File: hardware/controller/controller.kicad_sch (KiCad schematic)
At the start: 29 parts, among them J1 DC_12V_IN, J2 HDD_POWER_OUT, J3 470531000, J4 470531000, J5 Conn_01x07, Q1 2N3904, Q2 2N3904, U1 TSR0.5-2450, U2 XIAO-RP2350-SMD, U3 INA228, U4 74HC4051

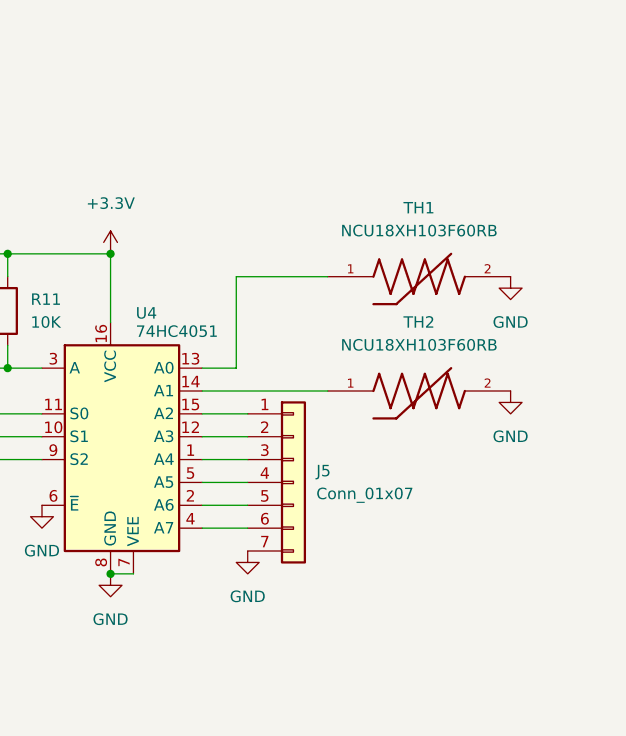
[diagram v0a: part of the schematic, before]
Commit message: swap out thermistor connector
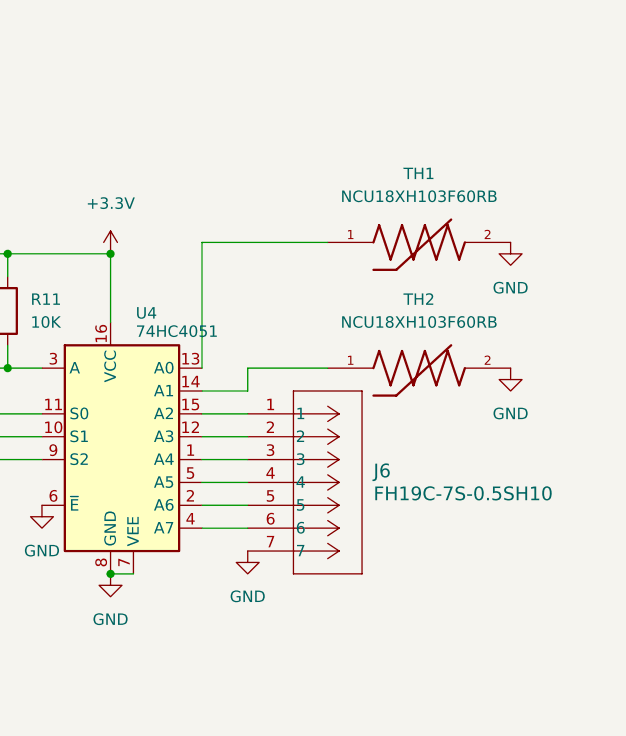
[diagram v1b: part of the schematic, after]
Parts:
- removed J5: Conn_01x07, Connector_JST:JST_XH_B7B-XH-A_1x07_P2.50mm_Vertical, symbol Connector_Generic:Conn_01x07
- added J6: FH19C-7S-0.5SH10, CONN7_FH19C_7S_HIR, symbol Hirose_2026-10-24_22-08-50:FH19C-7S-0.5SH10
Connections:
- net GND: now also J6.7
- net at U4.1 (A4): now also J6.3
- net at U4.12 (A3): now also J6.2
- net at U4.15 (A2): now also J6.1
- net at U4.2 (A6): now also J6.5
- net at U4.4 (A7): now also J6.6
- net at U4.5 (A5): now also J6.4
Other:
- moved on the sheet: TH1, TH2

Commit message: update symbol and footprint libraries for thermistor strip
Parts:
- J6: footprint CONN7_FH19C_7S_HIR -> Hirose_FH19C_7S_0_5SH:CONN7_FH19C_7S_HIR
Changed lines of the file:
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@@
 			)
 		)
-		(property "Footprint" "CONN7_FH19C_7S_HIR"
+		(property "Footprint" "Hirose_FH19C_7S_0_5SH:CONN7_FH19C_7S_HIR"
 			(at 213.36 124.46 0)
 			(hide yes)

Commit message: fix shunt footprint
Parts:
- removed RSH1: 0.2m, CSS2H_3920R_L200F:RES_3920R_L200x_BRN, symbol CSS2H_3920R_L200F:CSS2H-3920R-L200F
- added RSH1: CRF2512-FZ-R001ELF, CRF2512-FZ-R001ELF:RESC6432X80N, symbol CRF2512-FZ-R001ELF:CRF2512-FZ-R001ELF
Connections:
- net 12V_HDD: now also RSH1.2
- net 12V_IN: now also RSH1.1
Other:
- moved on the sheet: R3

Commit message: first pass at placing components for fan controller on front face
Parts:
- RSH1: footprint CRF2512-FZ-R001ELF:RESC6432X80N -> CRF2512_FZ_R001ELF:RESC6432X80N
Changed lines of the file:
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@@
 			)
 		)
-		(property "Footprint" "CRF2512-FZ-R001ELF:RESC6432X80N"
+		(property "Footprint" "CRF2512_FZ_R001ELF:RESC6432X80N"
 			(at 152.4 59.69 0)
 			(hide yes)

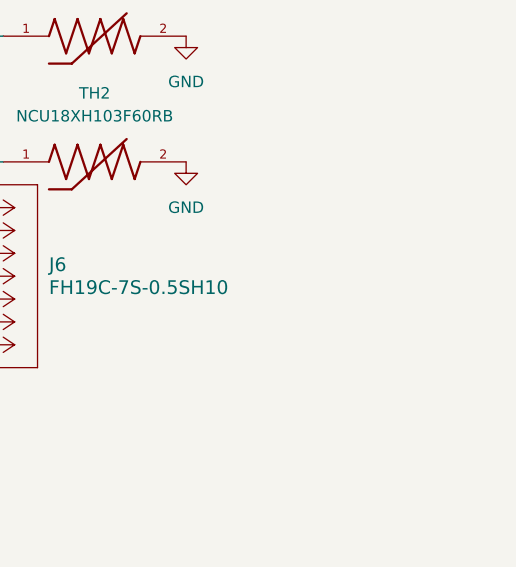
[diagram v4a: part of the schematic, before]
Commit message: initial attempt at tracing for controller, still need vias
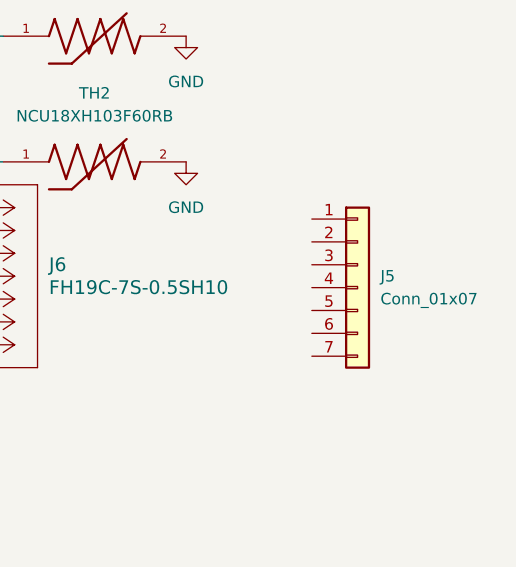
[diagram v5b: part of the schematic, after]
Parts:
- added J5: Conn_01x07, symbol Connector_Generic:Conn_01x07
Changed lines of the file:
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@@
+	)
+	(symbol
+		(lib_id "Connector_Generic:Conn_01x07")
+		(at 261.62 133.35 0)
+		(unit 1)
+		(body_style 1)
+		(exclude_from_sim no)
+		(in_bom yes)
+		(on_board yes)
+		(in_pos_files yes)
+		(dnp no)
+		(fields_autoplaced yes)
+		(property "Reference" "J5"
+			(at 264.16 132.0799 0)
+			(show_name no)
+			(do_not_autoplace no)
+			(effects
+				(font
+					(size 1.27 1.27)
+				)
+				(justify left)
+			)
+		)
+		(property "Value" "Conn_01x07"
+			(at 264.16 134.6199 0)
+			(show_name no)
+			(do_not_autoplace no)
+			(effects
+				(font
+					(size 1.27 1.27)
+				)
+				(justify left)
+			)
+		)
+		(property "Footprint" ""
+			(at 261.62 133.35 0)
+			(hide yes)
+			(show_name no)
+			(do_not_autoplace no)
+			(effects
+				(font
+					(size 1.27 1.27)
+				)
+			)
+		)
+		(property "Datasheet" ""
+			(at 261.62 133.35 0)
+			(hide yes)
+			(show_name no)
+			(do_not_autoplace no)
+			(effects
+				(font
+					(size 1.27 1.27)
+				)
+			)
+		)
+		(property "Description" "Generic connector, single row, 01x07, script generated (kicad-library-utils/schlib/autogen/connector/)"
+			(at 261.62 133.35 0)
+			(hide yes)
+			(show_name no)
+			(do_not_autoplace no)
+			(effects
+				(font
+					(size 1.27 1.27)
+				)
+			)
+		)
+		(pin "2"
+		)
+		(pin "1"
+		)
+		(pin "3"
+		)
+		(pin "4"
+		)
+		(pin "7"
+		)
+		(pin "6"
+		)
+		(pin "5"
+		)
+		(instances
+			(project "controller"
+				(path "/2efa048c-d6c1-446c-ae8e-880d974401eb"
+					(reference "J5")
+					(unit 1)
+				)
+			)
+		)
 	)
 	(symbol

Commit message: finish routes for INA228
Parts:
- added NT1, NT2: NetTie_2, NetTie:NetTie-2_SMD_Pad0.5mm, symbol Device:NetTie_2
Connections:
- net 12V_HDD: now also RSH1.1, NT2.1; no longer R4.1, RSH1.2, U3.8 (Vbus)
- net 12V_IN: now also RSH1.2, NT1.1; no longer R3.1, RSH1.1
- net FAN1_PWM: now also U2.9 (D8); no longer U2.8 (D7)
- net FAN1_TACH: now also U2.8 (D7); no longer U2.9 (D8)
- net FAN2_PWM: now also U2.11 (D10); no longer U2.10 (D9)
- net FAN2_TACH: now also U2.10 (D9); no longer U2.11 (D10)
- net NTC_SEL0: now also U2.7 (D6); no longer U2.3 (D2)
- net NTC_SEL2: now also U2.3 (D2); no longer U2.7 (D6)
- new net 12V_HDD_SENSE: NT2.2, R4.1, U3.8 (Vbus)
- new net 12V_IN_SENSE: NT1.2, R3.1
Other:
- moved on the sheet: C2, R3, RSH1

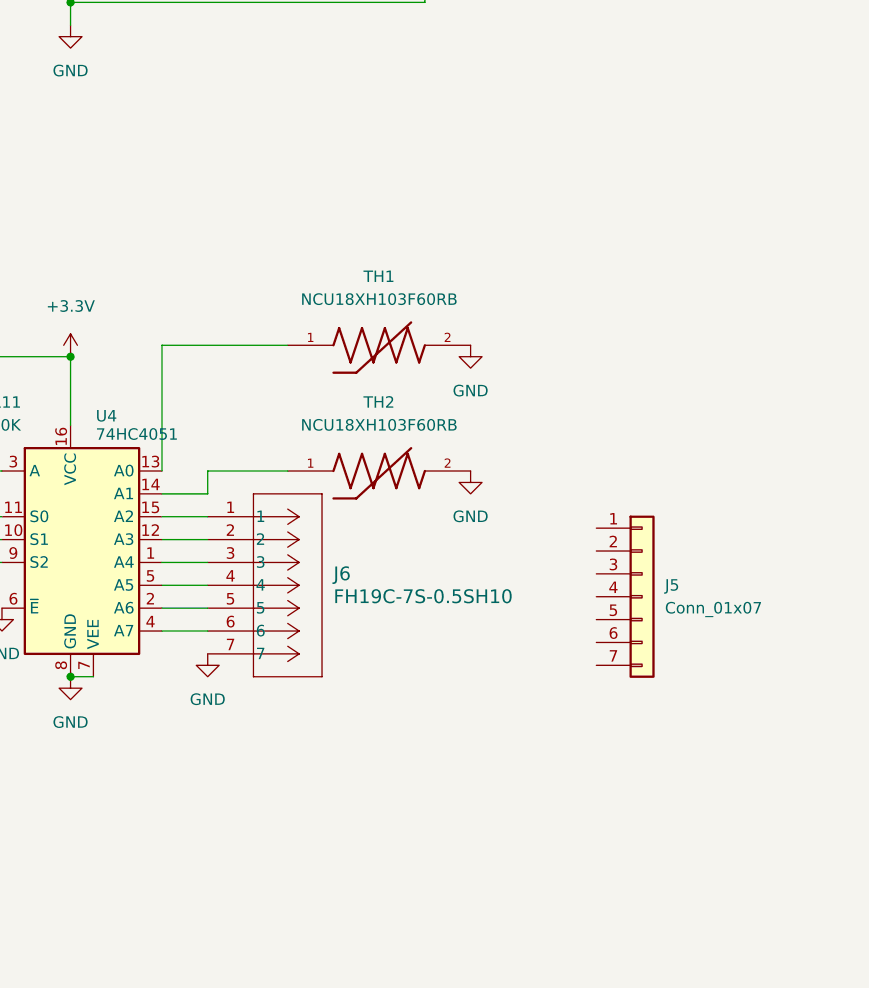
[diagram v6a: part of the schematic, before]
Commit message: add mounting holes
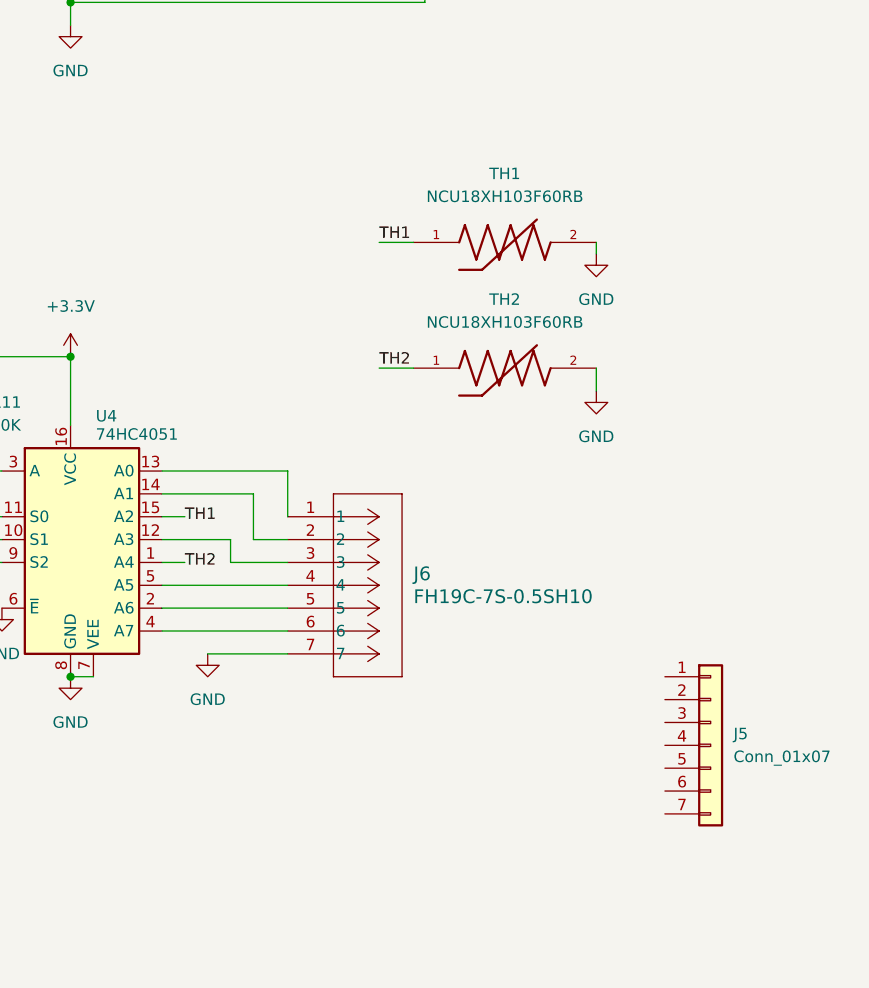
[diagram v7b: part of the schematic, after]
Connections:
- net at J6.3: now also U4.12 (A3); no longer U4.1 (A4)
- net at J6.2: now also U4.14 (A1); no longer U4.12 (A3)
- net at U4.13 (A0): now also J6.1; no longer TH1.1
- net TH2: now reaches TH2.1
- net TH2: now also U4.1 (A4); no longer U4.14 (A1)
- net TH1: now reaches U4.15 (A2)
- net TH1: now also TH1.1; no longer J6.1
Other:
- moved on the sheet: J5, J6, TH1, TH2

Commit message: footprint template for JST
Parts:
- removed J6: FH19C-7S-0.5SH10, Hirose_FH19C_7S_0_5SH:CONN7_FH19C_7S_HIR, symbol Hirose_2026-10-24_22-08-50:FH19C-7S-0.5SH10
- J5: footprint (none) -> Connector_JST:JST_ZH_S7B-ZR-SM4A-TF_1x07-1MP_P1.50mm_Horizontal
- renumbered TH1 to TH7, TH2 to TH8
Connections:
- net GND: now also J5.5 (Pin_5)
- net TH1: now also J5.1 (Pin_1), U4.1 (A4); no longer TH7.1, U4.15 (A2)
- net TH2: now also J5.2 (Pin_2), U4.2 (A6); no longer TH8.1, U4.1 (A4)
- net TH5: now reaches U4.12 (A3)
- net TH5: now also J5.6 (Pin_6)
- net TH6: now reaches U4.13 (A0)
- net TH6: now also J5.7 (Pin_7)
- net TH8: now reaches U4.14 (A1)
- net TH8: now also TH8.1
- net TH3: now reaches U4.4 (A7)
- net TH3: now also J5.3 (Pin_3)
- net TH4: now reaches U4.5 (A5)
- net TH4: now also J5.4 (Pin_4)
- new net TH7: TH7.1, U4.15 (A2)
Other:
- moved on the sheet: J5
